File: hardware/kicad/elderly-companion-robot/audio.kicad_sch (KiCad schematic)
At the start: 7 parts, among them J10 Speaker, J9 INMP441_Mic, U8 MAX98357A

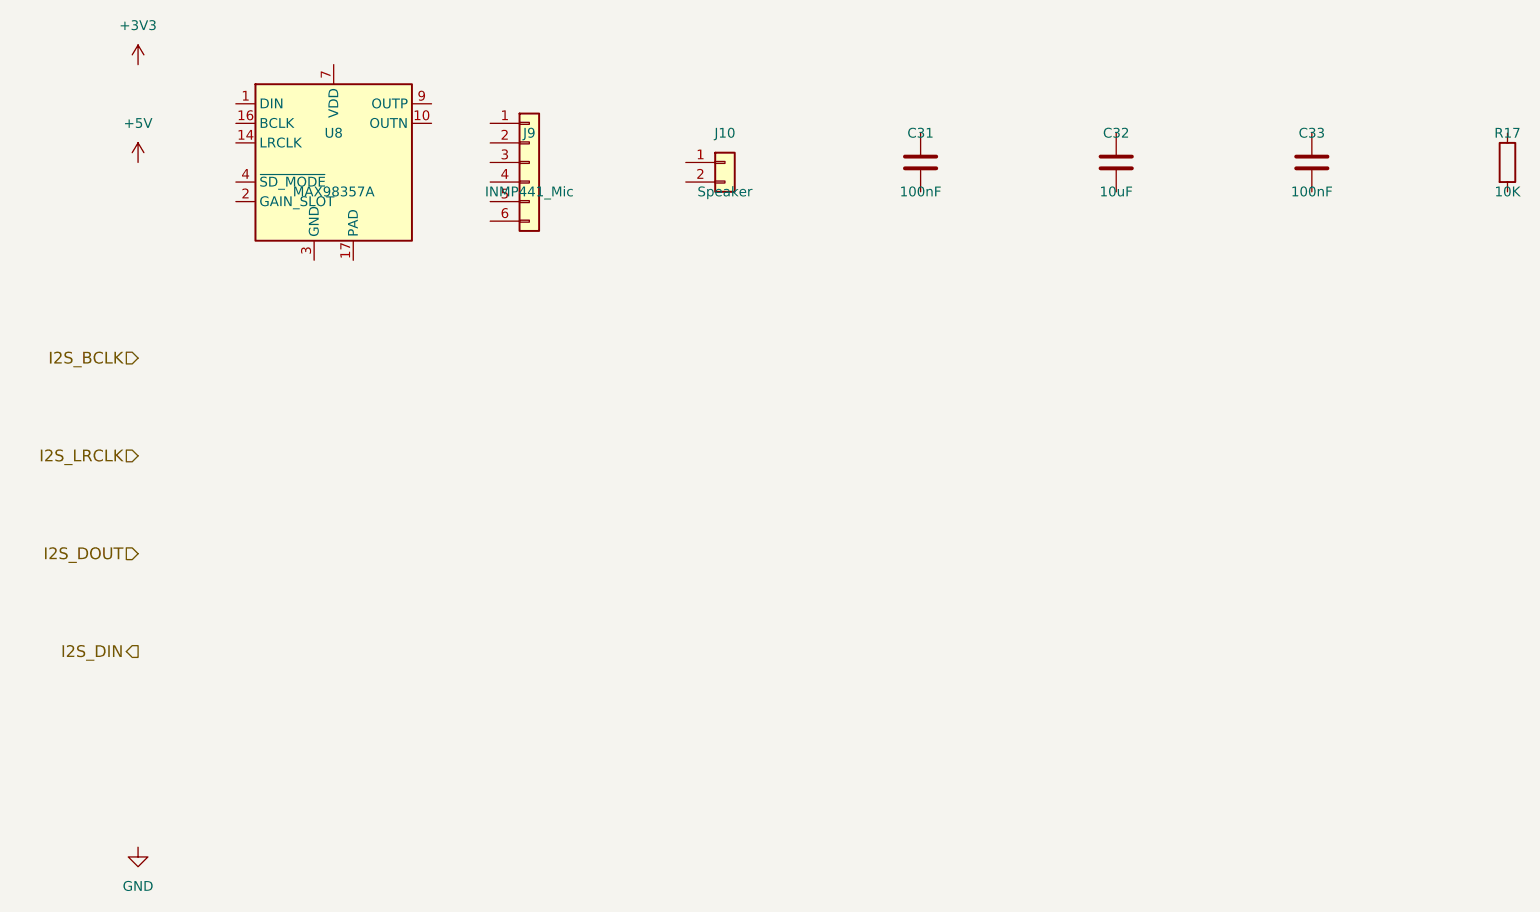
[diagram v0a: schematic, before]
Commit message: Add net labels and signal connections across all schematic sheets
- MCU Core: Added net labels at all ESP32-S3 GPIO pin positions
  (I2C, I2S, motor, servo, IR, UART, ultrasonic signals)
- Added hierarchical labels for US_LEFT/RIGHT_TRIG/ECHO
- Remapped I2C_SCL to GPIO2 (GPIO22 not on WROOM-1 module)
- Remapped SERVO_PAN to GPIO42 (GPIO44 not available)
- Motor Driver: Added net labels at L298N input/output pins
- Sensors: Added I2C labels at MPU-6050 and SSD1306 pin positions
- Audio: Added I2S labels at MAX98357A and INMP441 connector
- Camera/Dock: Added UART, SIM_PWRKEY, servo, IR labels at SIM800C
- Added power symbols (+3V3, +5V, GND, +4V) across all sheets
- Boot circuit wiring started (EN pull-up, GPIO0 connections)
- ERC: 446 violations (mostly unconnected labels/pins - need wires)

Co-Authored-By: Claude Opus 4.7 <noreply@anthropic.com>
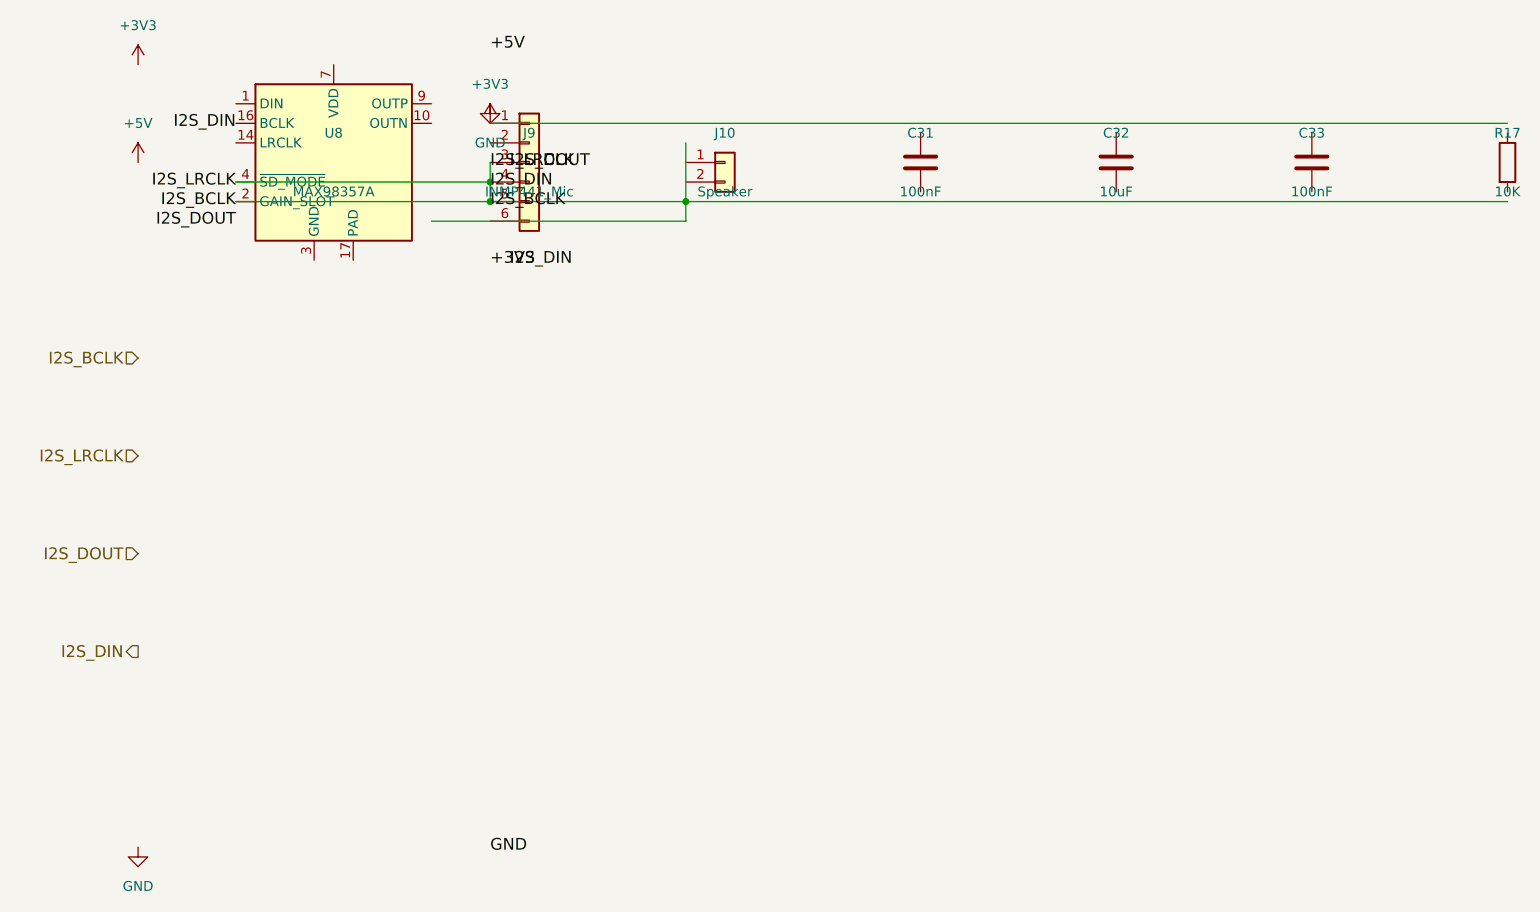
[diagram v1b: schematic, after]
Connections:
- net +3V3: now also J9.1 (Pin_1)
- net I2S_BCLK: now also J9.3 (Pin_3), J9.4 (Pin_4), J9.5 (Pin_5), U8.16 (BCLK), U8.2 (GAIN_SLOT), U8.4 (~{SD_MODE})
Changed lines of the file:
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@@
 	(version 20250114)
 	(generator "eeschema")
+	(generator_version "9.0")
 	(paper "A4")
 	(symbol
@@
 		(effects (font (size 1.524 1.524)))
 	)
+	(junction (at 71.12 53.34)
+		(diameter 0)
+	)
+	(junction (at 71.12 55.88)
+		(diameter 0)
+	)
+	(junction (at 96.52 55.88)
+		(diameter 0)
+	)
+	(label "I2S_DOUT"
+		(at 73.66 50.8 0)
+		(effects (font (size 1.524 1.524)))
+	)
+	(label "I2S_DIN"
+		(at 73.66 63.5 0)
+		(effects (font (size 1.524 1.524)))
+	)
+	(label "+5V"
+		(at 71.12 35.56 0)
+		(effects (font (size 1.524 1.524)))
+	)
+	(label "+3V3"
+		(at 71.12 63.5 0)
+		(effects (font (size 1.524 1.524)))
+	)
+	(label "GND"
+		(at 71.12 139.7 0)
+		(effects (font (size 1.524 1.524)))
+	)
+	(label "I2S_DOUT"
+		(at 38.1 58.42 180)
+		(effects (font (size 1.524 1.524)))
+	)
+	(label "I2S_LRCLK"
+		(at 38.1 53.34 180)
+		(effects (font (size 1.524 1.524)))
+	)
+	(label "I2S_BCLK"
+		(at 38.1 55.88 180)
+		(effects (font (size 1.524 1.524)))
+	)
+	(label "I2S_DIN"
+		(at 38.1 45.72 180)
+		(effects (font (size 1.524 1.524)))
+	)
+	(label "I2S_DIN"
+		(at 71.12 53.34 0)
+		(effects (font (size 1.524 1.524)))
+	)
+	(label "I2S_BCLK"
+		(at 71.12 55.88 0)
+		(effects (font (size 1.524 1.524)))
+	)
+	(label "I2S_LRCLK"
+		(at 71.12 50.8 0)
+		(effects (font (size 1.524 1.524)))
+	)
+	(symbol
+		(lib_id "power:+3V3")
+		(at 71.12 45.72 0)
+		(unit 1)
+		(exclude_from_sim no)
+		(in_bom yes)
+		(on_board yes)
+		(dnp no)
+		(property "Reference" "#PWRf031"
+			(at 71.12 39.37 0)
+			(effects (font (size 1.27 1.27)) (hide yes))
+		)
+		(property "Value" "+3V3"
+			(at 71.12 40.64 0)
+			(effects (font (size 1.27 1.27)))
+		)
+		(property "Footprint" ""
+			(at 71.12 45.72 0)
+			(effects (font (size 1.27 1.27)) (hide yes))
+		)
+		(property "Datasheet" "~"
+			(at 71.12 45.72 0)
+			(effects (font (size 1.27 1.27)) (hide yes))
+		)
+		(instances
+			(project "elderly-companion-robot"
+				(path "/325b14b3-5b6b-4ebf-9147-f3f960e0337e"
+					(reference "#PWRf031") (unit 1)
+				)
+			)
+		)
+	)
+	(symbol
+		(lib_id "power:GND")
+		(at 71.12 43.18 0)
+		(unit 1)
+		(exclude_from_sim no)
+		(in_bom yes)
+		(on_board yes)
+		(dnp no)
+		(property "Reference" "#PWR4b09"
+			(at 71.12 49.53 0)
+			(effects (font (size 1.27 1.27)) (hide yes))
+		)
+		(property "Value" "GND"
+			(at 71.12 48.26 0)
+			(effects (font (size 1.27 1.27)))
+		)
+		(property "Footprint" ""
+			(at 71.12 43.18 0)
+			(effects (font (size 1.27 1.27)) (hide yes))
+		)
+		(property "Datasheet" "~"
+			(at 71.12 43.18 0)
+			(effects (font (size 1.27 1.27)) (hide yes))
+		)
+		(instances
+			(project "elderly-companion-robot"
+				(path "/d531ab51-ca87-4987-8efe-123157564a06"
+					(reference "#PWR4b09") (unit 1)
+				)
+			)
+		)
+	)
+	(wire
+		(pts (xy 71.12 45.72) (xy 203.2 45.72))
+		(stroke (width 0) (type solid))
+	)
+	(wire
+		(pts (xy 38.1 53.34) (xy 71.12 53.34))
+		(stroke (width 0) (type solid))
+	)
+	(wire
+		(pts (xy 38.1 55.88) (xy 203.2 55.88))
+		(stroke (width 0) (type solid))
+	)
+	(wire
+		(pts (xy 63.5 58.42) (xy 96.52 58.42))
+		(stroke (width 0) (type solid))
+	)
+	(wire
+		(pts (xy 71.12 50.8) (xy 71.12 55.88))
+		(stroke (width 0) (type solid))
+	)
+	(wire
+		(pts (xy 96.52 48.26) (xy 96.52 58.42))
+		(stroke (width 0) (type solid))
+	)
 	(sheet_instances
